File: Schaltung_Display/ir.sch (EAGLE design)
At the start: 22 parts, among them IC1 ULN2003AN, IC2 LM324P, X1 22-23-2021, X2 22-23-2021, X3 22-23-2021, X5 22-23-2021

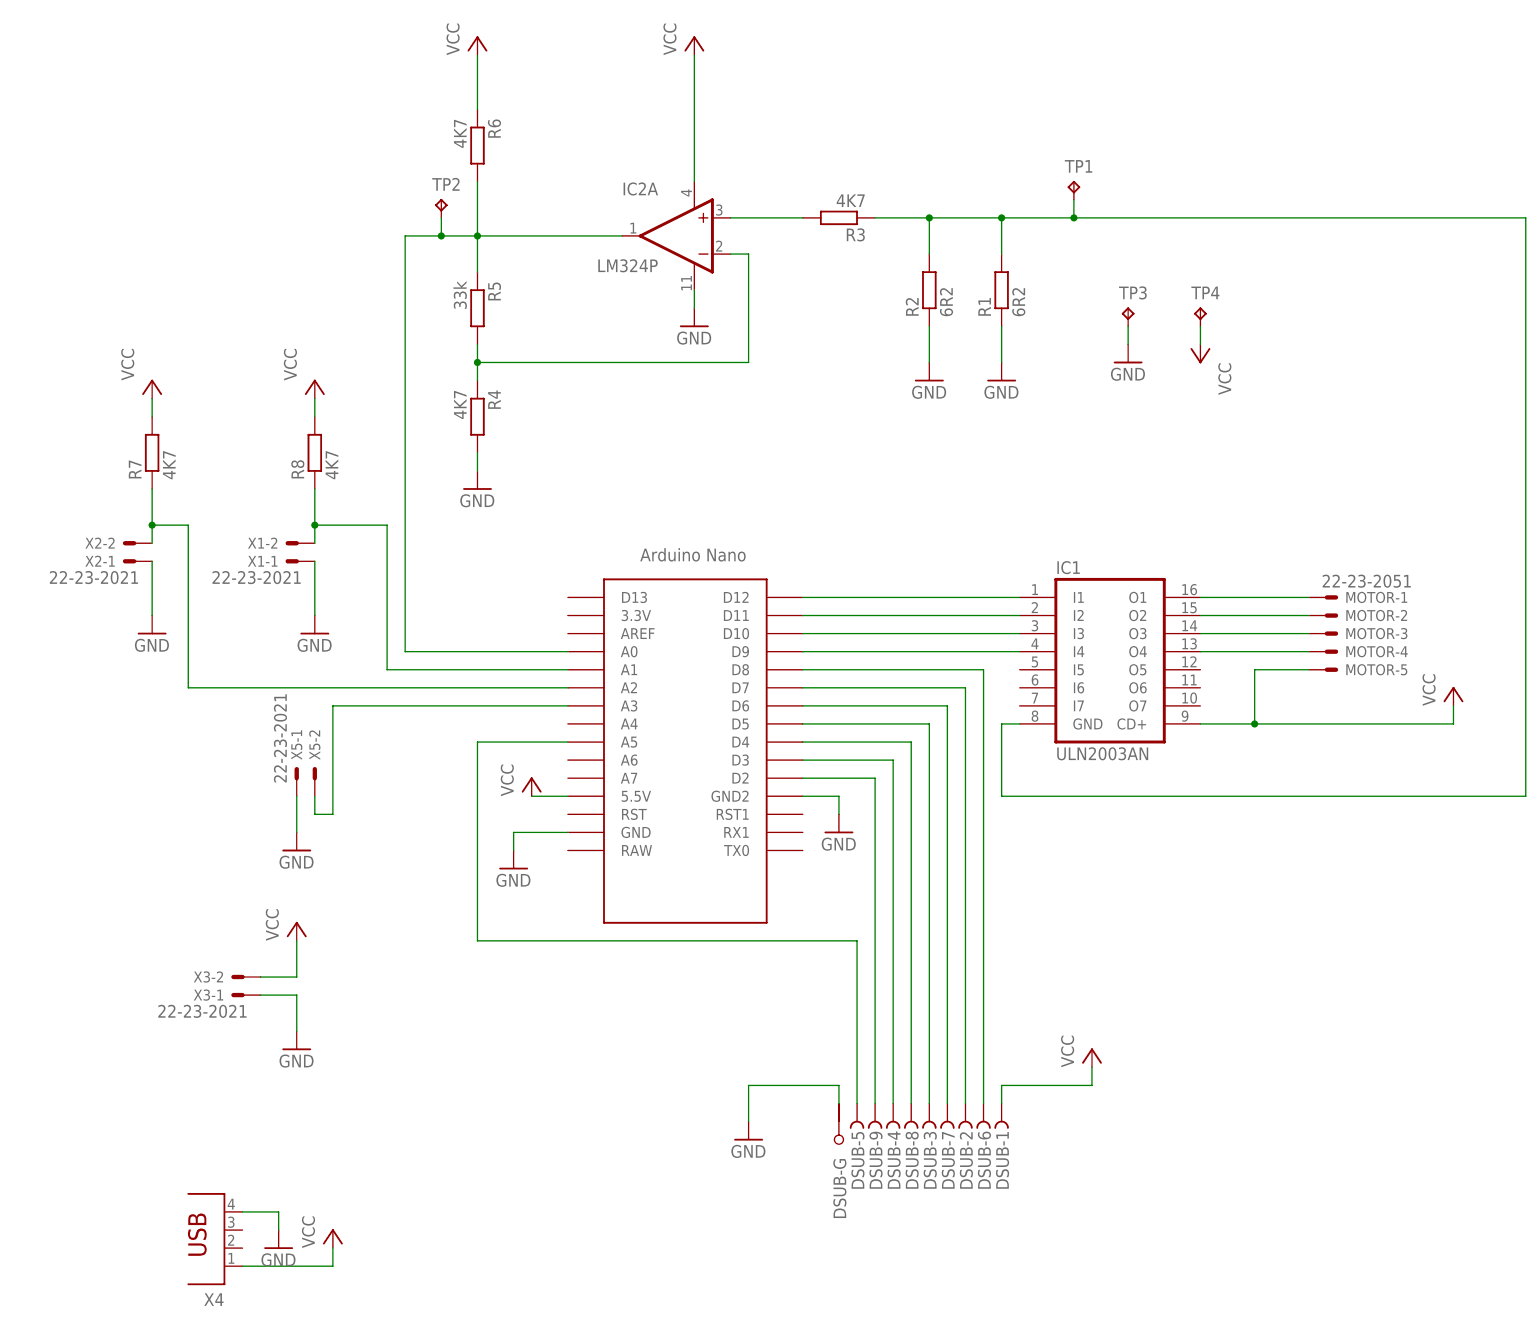
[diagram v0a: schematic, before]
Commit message: Update 3
Added electric cirquit diagrams,
pin-routing-table,
description of  IR-Module
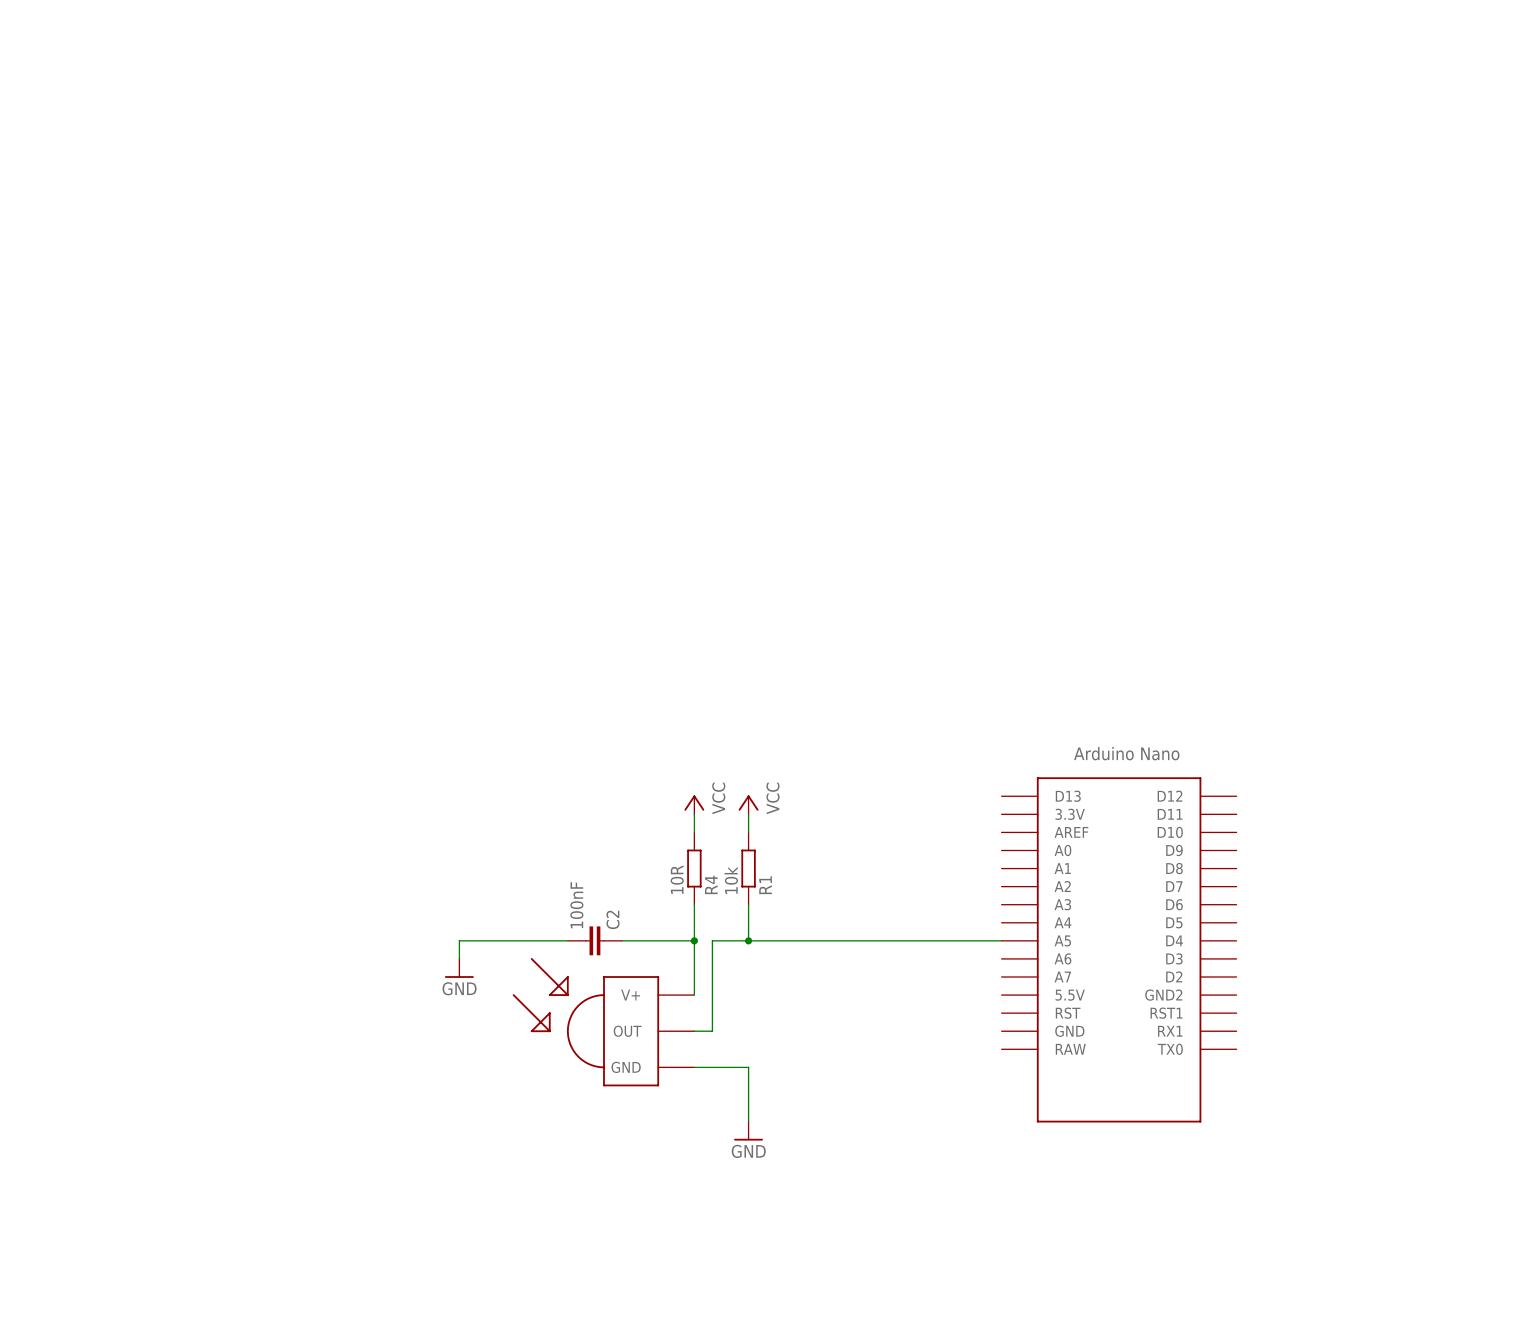
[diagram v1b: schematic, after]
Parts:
- removed DSUB: (no value), con-subd:F09HPS
- removed IC1: ULN2003AN, uln-udn:ULN2003AN
- removed IC2: LM324P, lm324:LM324P
- removed MOTOR: 22-23-2051, con-molex:22-23-2051
- removed R2: 6R2, rcl:R-EU_0207/10
- removed R3, R6, R7, R8: 4K7, rcl:R-EU_0207/10
- removed R5: 33k, rcl:R-EU_0207/10
- removed TP1, TP2, TP3, TP4: TPB2,54, testpad:TPB2,54
- removed X1, X2, X3, X5: 22-23-2021, con-molex:22-23-2021
- removed X4: (no value), con-berg:PN87520
- added C2: 100nF, rcl:C-EU025-025X050
- added U$2: NANO, Arduino-clone:NANO
- R1: value 6R2 -> 10k
- R4: value 4K7 -> 10R
- U$1: value NANO -> TSOP4838; device Arduino-clone:NANO -> tsop:TSOP4838
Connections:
- removed net N$1: IC1.O1, MOTOR-1.S
- removed net N$11: DSUB-7.F, U$1.D6
- removed net N$12: DSUB-3.F, U$1.D5
- removed net N$13: DSUB-8.F, U$1.D4
- removed net N$14: DSUB-4.F, U$1.D3
- removed net N$15: DSUB-9.F, U$1.D2
- removed net N$16: DSUB-6.F, U$1.D8
- removed net N$17: IC2A.+IN, R3.2
- removed net N$18: IC2A.OUT, R5.1, R6.2, TP2.TP, U$1.A0
- removed net N$19: IC2A.-IN, R4.1, R5.2
- removed net N$2: IC1.I1, U$1.D12
- removed net N$20: DSUB-5.F, U$1.A5
- removed net N$21: R8.1, U$1.A1, X1-2.S
- removed net N$22: R7.1, U$1.A2, X2-2.S
- removed net N$24: U$1.A3, X5-2.S
- removed net N$3: IC1.I2, U$1.D11
- removed net N$4: IC1.I3, U$1.D10
- removed net N$5: IC1.I4, U$1.D9
- removed net N$6: IC1.O2, MOTOR-2.S
- removed net N$8: IC1.O4, MOTOR-4.S
- removed net N$9: IC1.GND, R1.2, R2.2, R3.1, TP1.TP
- net GND: now also C2.2; no longer DSUB-G.G1, IC2A.V-, R1.1, R2.1, R4.2, TP3.TP, U$1.GND2, X1-1.S, X2-1.S, X3-1.S, X4.4, X5-1.S
- net N$10: now also C2.1, R4.1, U$1.V+; no longer DSUB-2.F, U$1.D7
- net N$7: now also R1.1, U$1.OUT, U$2.A5; no longer IC1.O3, MOTOR-3.S
- net VCC: now also R1.2, R4.2; no longer DSUB-1.F, IC1.CD+, IC2A.V+, MOTOR-5.S, R6.1, R7.2, R8.2, TP4.TP, U$1.5.5V, X3-2.S, X4.1
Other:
- moved on the sheet: R1, R4
